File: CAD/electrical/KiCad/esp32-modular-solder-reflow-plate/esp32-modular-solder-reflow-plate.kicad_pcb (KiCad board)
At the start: 2 copper layers, 81.3 x 50.8 mm, 100 parts, among them J1 Micro_SD, J2 USB-C, J3 I2C, J4 Thermo Coupler, J5 Heater, J6 PWR_IN, J7 Serial, J8 Buzzer, Q1 Heater N-FET, Q2 Q_PMOS_DGS, Q3 BUZ_CTL, SW1 µC_BTN01, SW2 µC_BTN02, SW3 µC_BTN03, SW4 µC_BTN04, SW5 µC_EN, SW6 µC_IO0, U1 MAX31855KASA, U2 ESP32-S3-WROOM-2, U3 AMS1117-3.3, U4 AMS1117-5.0, Y1 32k Hz

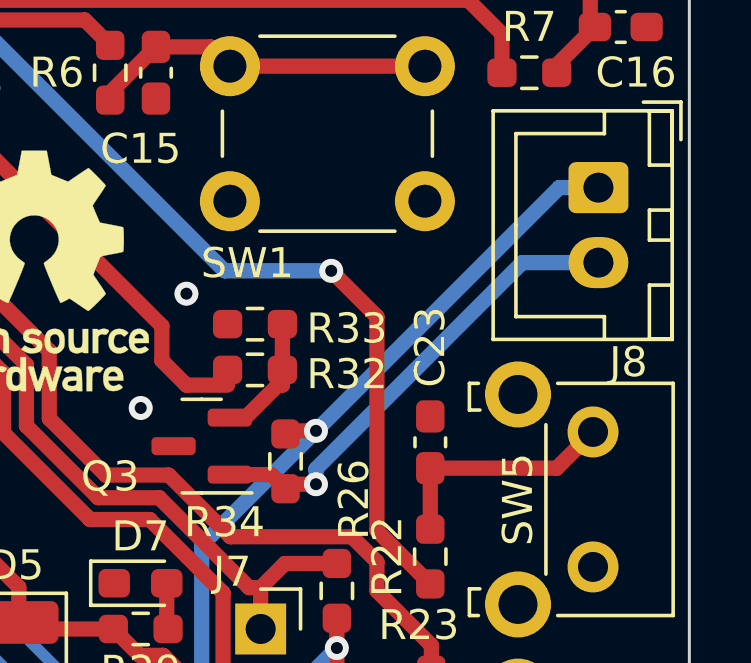
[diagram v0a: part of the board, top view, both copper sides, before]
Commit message: - cad: added bypass cap for the buzzer
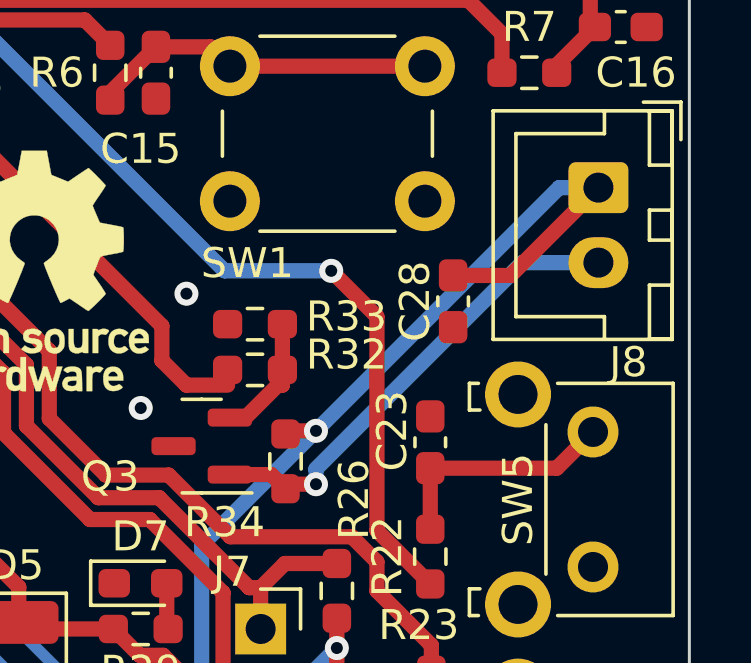
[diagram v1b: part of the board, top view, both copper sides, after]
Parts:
- added C28: 4µ7, Capacitor_SMD:C_0603_1608Metric_Pad1.08x0.95mm_HandSolder, F.Cu at (196.6, 84.3)
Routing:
- net +5V: track 150.1 -> 156.1 mm

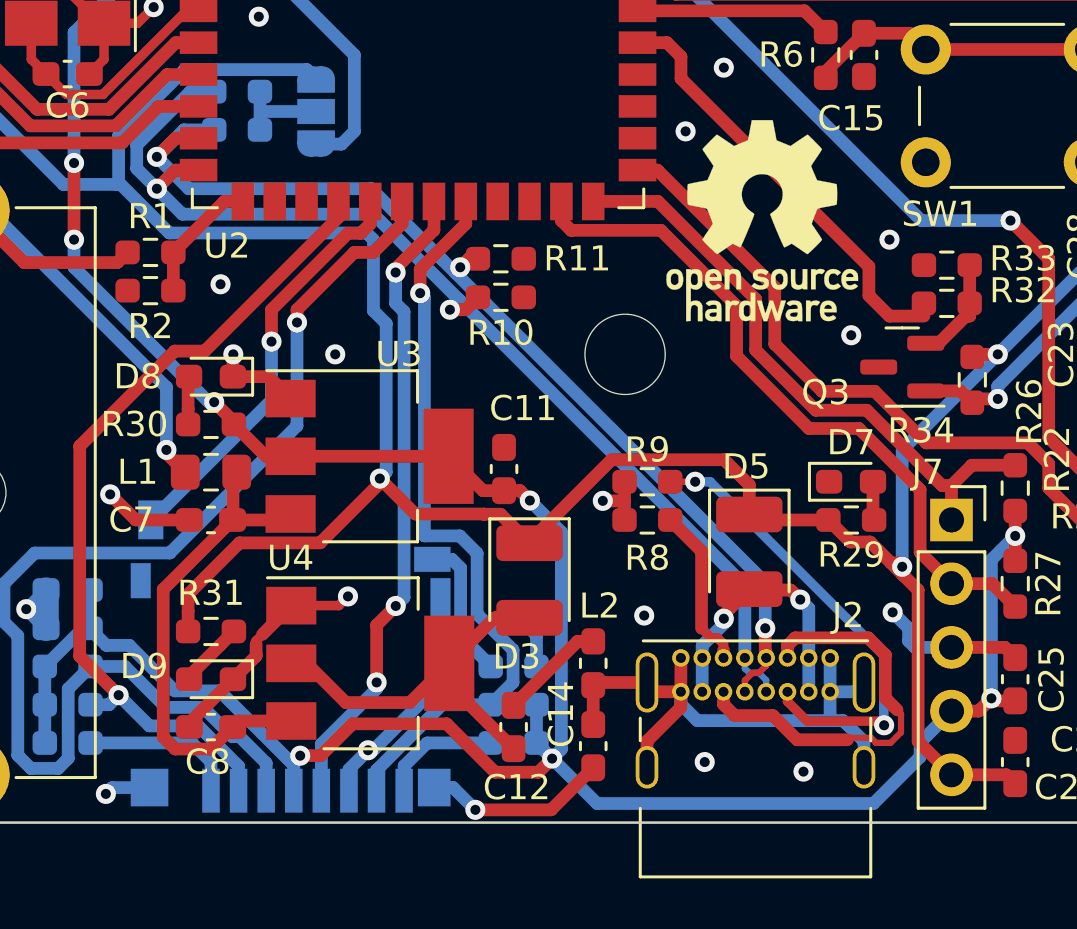
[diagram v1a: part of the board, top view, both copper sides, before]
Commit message: - cad: fixed usb c sbu pins; improved usb c slot routing
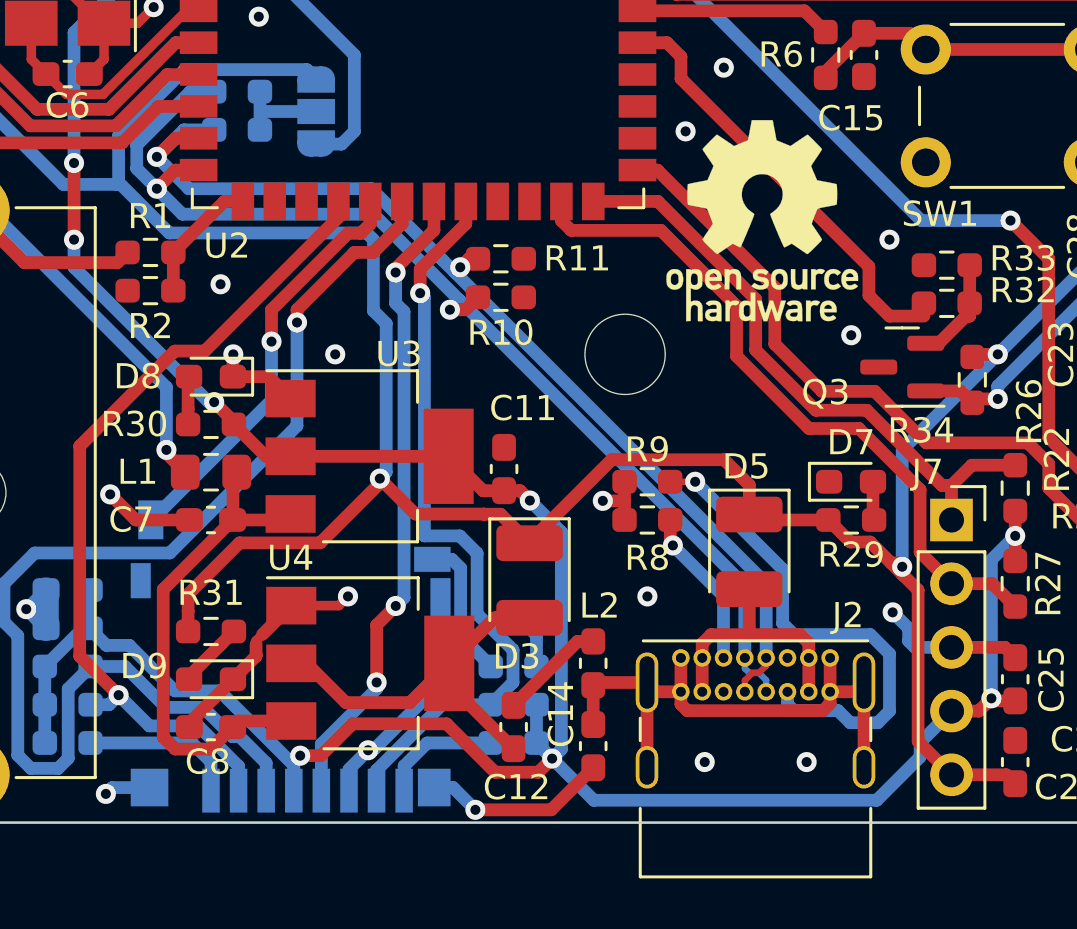
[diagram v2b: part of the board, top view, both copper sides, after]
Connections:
- J2 pad A8: USBC_SBU12 -> USBC_SBU1
- J2 pad B8: USBC_SBU12 -> USBC_SBU2
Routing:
- net USBC_SBU12: track 16.6 -> 0.00 mm
- net USBC_CC2: track 18.8 -> 20.2 mm, vias 2 -> 1
- net Net-(D5-A): track 10.9 -> 10.3 mm, vias 2 -> 0
- net USBC_CC1: track 6.83 -> 6.38 mm, vias 0 -> 1
- net USB_Dn: vias 3 -> 2

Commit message: - cad: add an auxiliary temperature probe input
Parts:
- added C7: 10n, Capacitor_SMD:C_0603_1608Metric_Pad1.08x0.95mm_HandSolder, B.Cu at (129.2, 62.2)
- added C8: 100n, Capacitor_SMD:C_0603_1608Metric_Pad1.08x0.95mm_HandSolder, F.Cu at (131.8, 69.0)
- added J5: Thermo Coupler, Connector_JST:JST_XH_B2B-XH-A_1x02_P2.50mm_Vertical, F.Cu at (127.1, 61.0)
- added U3: MAX31855KASA, Package_SO:SOIC-8_3.9x4.9mm_P1.27mm, F.Cu at (133.9, 65.4)
- C2, C28: moved to B.Cu
- J4: value Thermo Coupler -> Aux Thermo Coupler
- moved C5 7.26 mm to (133.2, 76.1), turned to 0 degrees
- moved R30 6.86 mm to (195.3, 84.3), turned to -90 degrees
- moved D6 6.84 mm to (134.6, 59.1)
- moved Q3 6.48 mm to (192.5, 84.3), turned to 0 degrees
- moved C28 5.53 mm to (199.5, 79.6), turned to 90 degrees
- moved R31 5.40 mm to (135.8, 61.9)
- moved R26 2.90 mm to (192.3, 88.4)
- moved R27 2.90 mm to (192.3, 86.9), turned to 180 degrees
- moved C2 1.88 mm to (129.2, 70.6)
- moved U1 1.37 mm to (133.9, 72.5), turned to 0 degrees
- moved REF** 1.02 mm to (182.5, 84.3)
- moved C30 0.75 mm to (131.1, 59.4), turned to -90 degrees
- moved C4 0.13 mm to (154.9, 71.2)
- moved C6 0.13 mm to (154.9, 77.3)
- renumbered C8 to C10, C9 to C11, C10 to C12, C11 to C13, C12 to C14, C13 to C15, C14 to C16, C15 to C17, C16 to C18, C17 to C19, C18 to C20, C19 to C21, C20 to C22, C21 to C23, C22 to C24, C23 to C25, C24 to C26, C25 to C27, C26 to C29, C27 to C30, C7 to C9, J5 to J6, J6 to J7, J7 to J8, J8 to J9, R32 to R26, R33 to R27, R26 to R28, R27 to R29, R34 to R30, R28 to R31, R29 to R32, R30 to R33, R31 to R34, U3 to U4, U4 to U5
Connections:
- U2 pad 23: unconnected-(U2-GPIO21-Pad23) -> AUX_ADC_TEMP_CS
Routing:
- net AUX_ADC_TEMP_CS: track 0.00 -> 48.8 mm, vias 0 -> 2
- net 3V3_µC: track 172.5 -> 183.7 mm
- net ADC_TEMP_SO: track 29.2 -> 40.4 mm
- net PWR_IN_N: track 77.2 -> 85.9 mm, vias 55 -> 71
- net AUX_THCPL_n: track 0.00 -> 8.53 mm
- net THCPL_n: track 15.3 -> 7.48 mm
- net AUX_THCPL_p: track 0.00 -> 7.47 mm
- net Net-(J9-Pin_2): track 15.9 -> 10.5 mm, vias 1 -> 0
- net NEOPIXEL_DIN: track 31.8 -> 27.4 mm
- net EN: track 54.4 -> 50.2 mm
- net ADC_TEMP_SCK: track 31.1 -> 34.3 mm, vias 0 -> 2
- net ADC_TEMP_CS: track 29.8 -> 27.6 mm, vias 0 -> 2
- net +5V: track 156.1 -> 154.0 mm
- net BUZZER_EN: track 17.1 -> 18.8 mm
- net USB_Dn: track 41.7 -> 43.3 mm
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
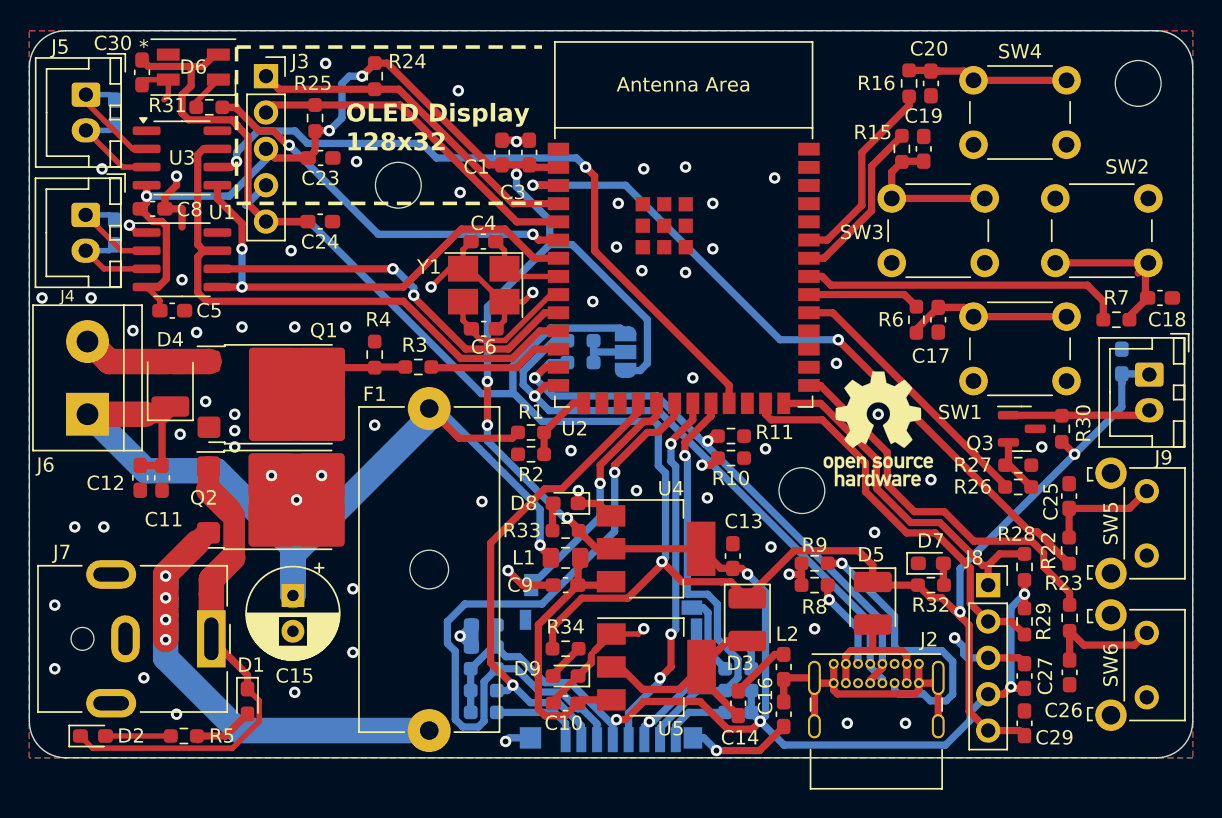
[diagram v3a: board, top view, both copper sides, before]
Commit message: - CAD: added usb pd trigger configurable via esp, routing adjustments
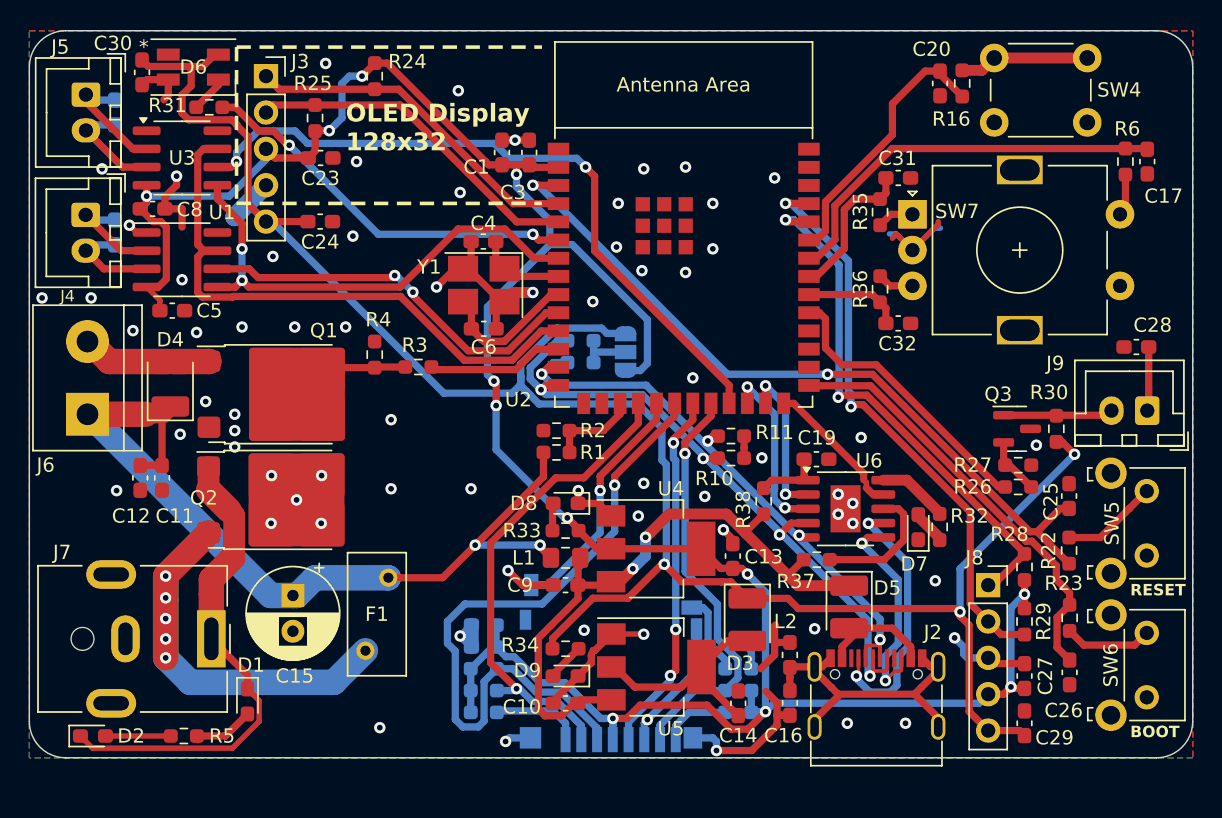
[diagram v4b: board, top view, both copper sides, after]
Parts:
- removed C18: 1µ, Capacitor_SMD:C_0603_1608Metric_Pad1.08x0.95mm_HandSolder
- removed Mount 1: MountingHole_3.2mm_M3, MountingHole:MountingHole_3.2mm_M3
- removed Mount 2: MountingHole_3.2mm_M3, MountingHole:MountingHole_3.2mm_M3
- removed Mount 3: MountingHole_3.2mm_M3, MountingHole:MountingHole_3.2mm_M3
- removed R15, R7: 0, Resistor_SMD:R_0603_1608Metric_Pad0.98x0.95mm_HandSolder
- removed R8, R9: 5k1, Resistor_SMD:R_0603_1608Metric_Pad0.98x0.95mm_HandSolder
- removed REF**: OSHW-Logo_7.5x8mm_SilkScreen, Symbol:OSHW-Logo_7.5x8mm_SilkScreen
- removed SW1: µC_BTN01, Button_Switch_THT:SW_PUSH_6mm
- removed SW2: µC_BTN02, Button_Switch_THT:SW_PUSH_6mm
- removed SW3: µC_BTN03, Button_Switch_THT:SW_PUSH_6mm
- added C31: 1µ, Capacitor_SMD:C_0603_1608Metric_Pad1.08x0.95mm_HandSolder, F.Cu at (183.9, 66.8)
- added C32: 1µ, Capacitor_SMD:C_0603_1608Metric_Pad1.08x0.95mm_HandSolder, F.Cu at (183.9, 77.0)
- added R35: 1k, Resistor_SMD:R_0603_1608Metric_Pad0.98x0.95mm_HandSolder, F.Cu at (182.6, 69.2)
- added R36: 1k, Resistor_SMD:R_0603_1608Metric_Pad0.98x0.95mm_HandSolder, F.Cu at (182.6, 74.6)
- added R37: 10k, Resistor_SMD:R_0603_1608Metric_Pad0.98x0.95mm_HandSolder, F.Cu at (178.2, 93.5)
- added R38: 1k, Resistor_SMD:R_0603_1608Metric_Pad0.98x0.95mm_HandSolder, F.Cu at (174.5, 89.4)
- added SW7: RotaryEncoder_Switch_MP, Rotary_Encoder:RotaryEncoder_Alps_EC11E-Switch_Vertical_H20mm, F.Cu at (184.9, 69.3)
- added U6: CH224K, Package_SO:SSOP-10-1EP_3.9x4.9mm_P1mm_EP2.1x3.3mm, F.Cu at (180.2, 89.9)
- C28: moved to F.Cu
- D7: value LED_VBUS -> LED_PG
- F1: value 1.5A -> 4A; footprint Fuse:Fuseholder_Cylinder-5x20mm_Schurter_0031_8201_Horizontal_Open -> Fuse:Fuse_BelFuse_0ZRE0005FF_L8.3mm_W3.8mm
- J2: footprint Connector_USB:USB_C_Receptacle_GCT_USB4085 -> Connector_USB:USB_C_Receptacle_G-Switch_GT-USB-7010ASV
- R16, R23, R6: value 0 -> 1k
- R22: value 10k -> 1k
- moved C19 22.9 mm to (178.2, 86.5), turned to 0 degrees
- moved C17 18.3 mm to (201.3, 65.7), turned to -90 degrees
- moved R6 18.3 mm to (199.8, 65.7), turned to 90 degrees
- moved F1 7.14 mm to (146.7, 99.8)
- moved J2 4.47 mm to (182.4, 104.1)
- moved R32 4.11 mm to (186.8, 91.2), turned to -90 degrees
- moved R16 3.71 mm to (188.4, 60.2)
- moved D7 2.68 mm to (185.3, 91.2), turned to 90 degrees
- moved J9 2.52 mm to (201.3, 83.1), turned to 180 degrees
- moved R2 2.43 mm to (160.0, 84.5)
- moved R1 2.26 mm to (160.0, 86.0)
- moved SW4 2.13 mm to (190.6, 58.4)
- moved D5 1.67 mm to (180.5, 96.8)
- moved C28 1.44 mm to (200.5, 78.6), turned to 180 degrees
- moved L2 0.94 mm to (176.3, 100.1)
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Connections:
- C17 pad 1: PWR_IN_N -> BTN03
- C17 pad 2: Net-(C17-Pad2) -> PWR_IN_N
- C19 pad 1: PWR_IN_N -> Net-(U6-VDD)
- C19 pad 2: Net-(C19-Pad2) -> PWR_IN_N
- C20 pad 2: Net-(C20-Pad2) -> BTN04
- C25 pad 2: Net-(C25-Pad2) -> EN
- C26 pad 2: Net-(C26-Pad2) -> IO0
- D5 pad 1: +5V -> VDD
- R16 pad 2: Net-(C20-Pad2) -> Net-(R16-Pad2)
- R22 pad 2: Net-(C25-Pad2) -> Net-(R22-Pad2)
- R23 pad 2: Net-(C26-Pad2) -> Net-(R23-Pad2)
- R32 pad 1: +5V -> USB_PD_PG
- R6 pad 1: BTN01 -> Net-(R6-Pad1)
- R6 pad 2: Net-(C17-Pad2) -> BTN03
- SW4 pad 1: Net-(C20-Pad2) -> Net-(R16-Pad2)
- SW5 pad 1: Net-(C25-Pad2) -> Net-(R22-Pad2)
- SW6 pad 1: Net-(C26-Pad2) -> Net-(R23-Pad2)
- U2 pad 15: VIN_ADC -> unconnected-(U2-GPIO3/TOUCH3/ADC1_CH2-Pad15)
- U2 pad 17: unconnected-(U2-GPIO9/TOUCH9/ADC1_CH8/FSPIHD/SUBSPIHD-Pad17) -> VIN_ADC
- U2 pad 24: unconnected-(U2-GPIO47/SPICLK_P/SUBSPICLK_P_DIFF-Pad24) -> USB_PD_CFG3
- U2 pad 25: TX0 -> USB_PD_CFG2
- U2 pad 26: RX0 -> USB_PD_CFG1
- U2 pad 32: BTN01 -> BTN02
- U2 pad 33: BTN02 -> BTN01
- U2 pad 36: unconnected-(U2-U0RXD/GPIO44/CLK_OUT2-Pad36) -> RX0
- U2 pad 37: unconnected-(U2-U0TXD/GPIO43/CLK_OUT1-Pad37) -> TX0
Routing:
- net VDD: track 20.0 -> 45.1 mm, vias 0 -> 2
- net BTN03: track 11.9 -> 28.2 mm
- net BTN02: track 22.6 -> 6.83 mm
- net PWR_IN_N: track 85.9 -> 100.0 mm, vias 71 -> 70
- net Net-(C18-Pad2): track 12.9 -> 0.00 mm
- net RX0: track 24.4 -> 37.2 mm, vias 0 -> 2
- net TX0: track 27.9 -> 40.6 mm, vias 0 -> 2
- net USBC_CC1: track 6.38 -> 18.9 mm, vias 1 -> 2
- net USB_PD_CFG3: track 0.00 -> 12.4 mm, vias 0 -> 2
- net Net-(C17-Pad2): track 12.4 -> 0.00 mm
- net HEATER_P: track 71.8 -> 59.6 mm, vias 1 -> 2
- net Net-(C20-Pad2): track 11.4 -> 0.00 mm
- net USB_PD_CFG2: track 0.00 -> 10.9 mm, vias 0 -> 2
- net Net-(C19-Pad2): track 10.9 -> 0.00 mm
- net USB_PD_CFG1: track 0.00 -> 10.1 mm
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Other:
- board text added: "BOOT"
- board text added: "RESET"
